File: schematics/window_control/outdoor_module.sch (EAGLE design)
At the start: 25 parts, among them J1 J_SMD, J10 USBASP_PIN, J2 J_SMD, J3 J_SMD, U5 BMP280 5V module, U6 LM317L, U7 LM358, U8 ATMEGA328P, U9 GY-SGP30

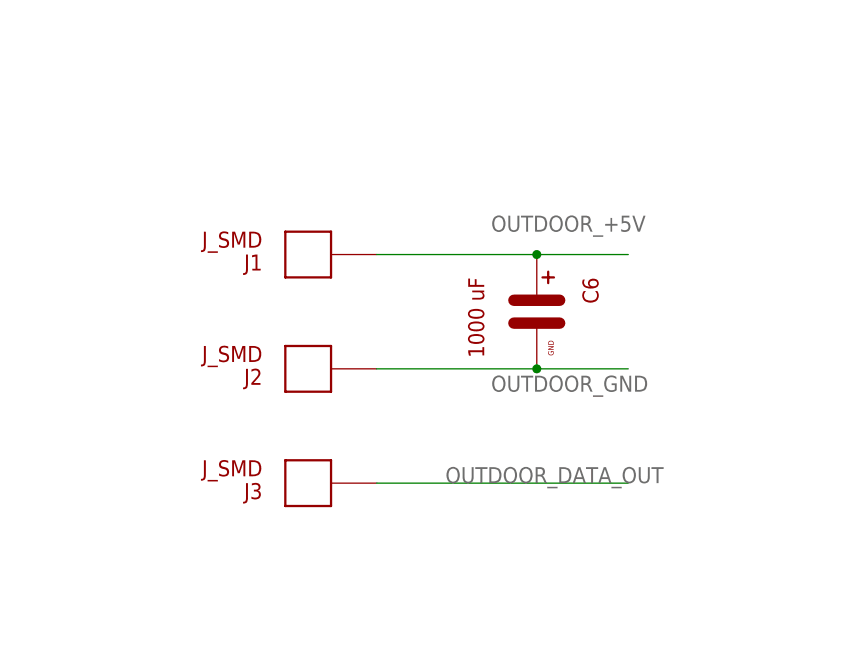
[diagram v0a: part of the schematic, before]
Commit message: Connectors changed
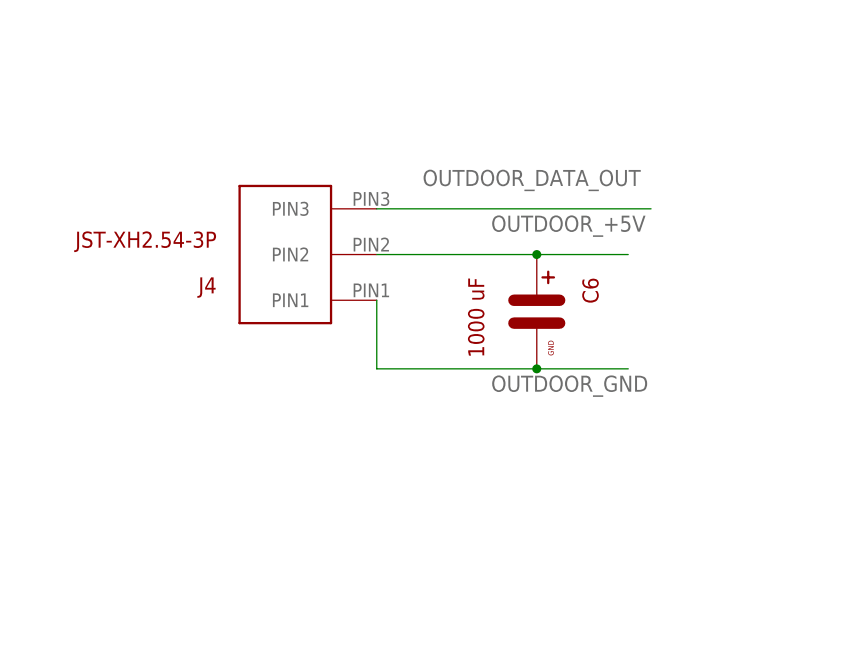
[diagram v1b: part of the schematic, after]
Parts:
- removed J1, J2, J3: J_SMD, my_devices:J_SMD
- added J4: JST-XH2.54-3P, my_devices:JST-XH254-3P
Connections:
- net OUTDOOR_+5V: now also J4.PIN2; no longer J1.PIN
- net OUTDOOR_DATA_OUT: now also J4.PIN3; no longer J3.PIN
- net OUTDOOR_GND: now also J4.PIN1; no longer J2.PIN
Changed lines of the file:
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@@
 <part name="C9" library="my_devices" deviceset="C-1" device="" value="0.1 uF"/>
 <part name="J10" library="my_devices" deviceset="USBASP_PIN" device=""/>
-<part name="J1" library="my_devices" deviceset="J_SMD" device=""/>
-<part name="J2" library="my_devices" deviceset="J_SMD" device=""/>
-<part name="J3" library="my_devices" deviceset="J_SMD" device=""/>
+<part name="J4" library="my_devices" deviceset="JST-XH254-3P" device="" value="JST-XH2.54-3P"/>
 </parts>
 <sheets>
@@
 <attribute name="VALUE" x="-103.505" y="208.915" size="0.8128" layer="94"/>
 </instance>
-<instance part="J1" gate="G$1" x="-297.18" y="264.16" smashed="yes" rot="R180" grouprefs="INPUT_CONNECTOR">
-<attribute name="NAME" x="-302.26" y="264.16" size="1.778" layer="94" rot="R180"/>
-<attribute name="VALUE" x="-302.26" y="266.7" size="1.778" layer="94" rot="R180"/>
-</instance>
-<instance part="J2" gate="G$1" x="-297.18" y="251.46" smashed="yes" rot="R180" grouprefs="INPUT_CONNECTOR">
-<attribute name="NAME" x="-302.26" y="251.46" size="1.778" layer="94" rot="R180"/>
-<attribute name="VALUE" x="-302.26" y="254" size="1.778" layer="94" rot="R180"/>
-</instance>
-<instance part="J3" gate="G$1" x="-297.18" y="238.76" smashed="yes" rot="R180" grouprefs="INPUT_CONNECTOR">
-<attribute name="NAME" x="-302.26" y="238.76" size="1.778" layer="94" rot="R180"/>
-<attribute name="VALUE" x="-302.26" y="241.3" size="1.778" layer="94" rot="R180"/>
+<instance part="J4" gate="G$1" x="-294.64" y="264.16" smashed="yes" rot="R180" grouprefs="INPUT_CONNECTOR">
+<attribute name="NAME" x="-307.34" y="261.62" size="1.778" layer="94" rot="R180"/>
+<attribute name="VALUE" x="-307.34" y="266.7" size="1.778" layer="94" rot="R180"/>
 </instance>
 </instances>
@@
 <junction x="-271.78" y="264.16" grouprefs="INPUT_CONNECTOR"/>
 <label x="-276.86" y="266.7" size="1.778" layer="95" grouprefs="INPUT_CONNECTOR"/>
-<pinref part="J1" gate="G$1" pin="PIN"/>
+<pinref part="J4" gate="G$1" pin="PIN2"/>
 </segment>
 <segment>
@@
 <junction x="-271.78" y="251.46" grouprefs="INPUT_CONNECTOR"/>
 <label x="-276.86" y="248.92" size="1.778" layer="95" grouprefs="INPUT_CONNECTOR"/>
-<pinref part="J2" gate="G$1" pin="PIN"/>
+<pinref part="J4" gate="G$1" pin="PIN1"/>
+<wire x1="-289.56" y1="259.08" x2="-289.56" y2="251.46" width="0.1524" layer="91" grouprefs="INPUT_CONNECTOR"/>
 </segment>
 <segment>
@@
 <net name="OUTDOOR_DATA_OUT" class="0">
 <segment>
-<wire x1="-289.56" y1="238.76" x2="-261.62" y2="238.76" width="0.1524" layer="91" grouprefs="INPUT_CONNECTOR"/>
-<label x="-281.94" y="238.76" size="1.778" layer="95" grouprefs="INPUT_CONNECTOR"/>
-<pinref part="J3" gate="G$1" pin="PIN"/>
-</segment>
-<segment>
+<wire x1="-289.56" y1="269.24" x2="-259.08" y2="269.24" width="0.1524" layer="91" grouprefs="INPUT_CONNECTOR"/>
+<label x="-284.48" y="271.78" size="1.778" layer="95" grouprefs="INPUT_CONNECTOR"/>
+<pinref part="J4" gate="G$1" pin="PIN3"/>
+</segment>
+<segment>

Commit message: Outdoor module board size reduced
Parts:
- U5: device my_devices:BME280 -> my_devices:BME280BME280-CONNECTOR-ONLY
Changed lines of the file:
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@@
 <grid distance="0.1" unitdist="inch" unit="inch" style="lines" multiple="1" display="no" altdistance="0.01" altunitdist="inch" altunit="inch"/>
 <layers>
-<layer number="1" name="Top" color="4" fill="1" visible="no" active="no"/>
-<layer number="2" name="Route2" color="1" fill="3" visible="no" active="no"/>
-<layer number="3" name="Route3" color="4" fill="3" visible="no" active="no"/>
-<layer number="4" name="Route4" color="1" fill="4" visible="no" active="no"/>
-<layer number="5" name="Route5" color="4" fill="4" visible="no" active="no"/>
-<layer number="6" name="Route6" color="1" fill="8" visible="no" active="no"/>
-<layer number="7" name="Route7" color="4" fill="8" visible="no" active="no"/>
-<layer number="8" name="Route8" color="1" fill="2" visible="no" active="no"/>
-<layer number="9" name="Route9" color="4" fill="2" visible="no" active="no"/>
-<layer number="10" name="Route10" color="1" fill="7" visible="no" active="no"/>
-<layer number="11" name="Route11" color="4" fill="7" visible="no" active="no"/>
-<layer number="12" name="Route12" color="1" fill="5" visible="no" active="no"/>
-<layer number="13" name="Route13" color="4" fill="5" visible="no" active="no"/>
-<layer number="14" name="Route14" color="1" fill="6" visible="no" active="no"/>
-<layer number="15" name="Route15" color="4" fill="6" visible="no" active="no"/>
-<layer number="16" name="Bottom" color="1" fill="1" visible="no" active="no"/>
-<layer number="17" name="Pads" color="2" fill="1" visible="no" active="no"/>
-<layer number="18" name="Vias" color="2" fill="1" visible="no" active="no"/>
-<layer number="19" name="Unrouted" color="6" fill="1" visible="no" active="no"/>
-<layer number="20" name="Dimension" color="24" fill="1" visible="no" active="no"/>
-<layer number="21" name="tPlace" color="7" fill="1" visible="no" active="no"/>
-<layer number="22" name="bPlace" color="7" fill="1" visible="no" active="no"/>
-<layer number="23" name="tOrigins" color="15" fill="1" visible="no" active="no"/>
-<layer number="24" name="bOrigins" color="15" fill="1" visible="no" active="no"/>
-<layer number="25" name="tNames" color="7" fill="1" visible="no" active="no"/>
-<layer number="26" name="bNames" color="7" fill="1" visible="no" active="no"/>
-<layer number="27" name="tValues" color="7" fill="1" visible="no" active="no"/>
-<layer number="28" name="bValues" color="7" fill="1" visible="no" active="no"/>
+<layer number="1" name="Top" color="4" fill="1" visible="yes" active="no"/>
+<layer number="2" name="Route2" color="16" fill="1" visible="yes" active="no"/>
+<layer number="3" name="Route3" color="17" fill="1" visible="yes" active="no"/>
+<layer number="4" name="Route4" color="18" fill="1" visible="yes" active="no"/>
+<layer number="5" name="Route5" color="19" fill="1" visible="yes" active="no"/>
+<layer number="6" name="Route6" color="25" fill="1" visible="yes" active="no"/>
+<layer number="7" name="Route7" color="26" fill="1" visible="yes" active="no"/>
+<layer number="8" name="Route8" color="27" fill="1" visible="yes" active="no"/>
+<layer number="9" name="Route9" color="28" fill="1" visible="yes" active="no"/>
+<layer number="10" name="Route10" color="29" fill="1" visible="yes" active="no"/>
+<layer number="11" name="Route11" color="30" fill="1" visible="yes" active="no"/>
+<layer number="12" name="Route12" color="20" fill="1" visible="yes" active="no"/>
+<layer number="13" name="Route13" color="21" fill="1" visible="yes" active="no"/>
+<layer number="14" name="Route14" color="22" fill="1" visible="yes" active="no"/>
+<layer number="15" name="Route15" color="23" fill="1" visible="yes" active="no"/>
+<layer number="16" name="Bottom" color="1" fill="1" visible="yes" active="no"/>
+<layer number="17" name="Pads" color="2" fill="1" visible="yes" active="no"/>
+<layer number="18" name="Vias" color="2" fill="1" visible="yes" active="no"/>
+<layer number="19" name="Unrouted" color="6" fill="1" visible="yes" active="no"/>
+<layer number="20" name="Dimension" color="24" fill="1" visible="yes" active="no"/>
+<layer number="21" name="tPlace" color="7" fill="1" visible="yes" active="no"/>
+<layer number="22" name="bPlace" color="7" fill="1" visible="yes" active="no"/>
+<layer number="23" name="tOrigins" color="15" fill="1" visible="yes" active="no"/>
+<layer number="24" name="bOrigins" color="15" fill="1" visible="yes" active="no"/>
+<layer number="25" name="tNames" color="7" fill="1" visible="yes" active="no"/>
+<layer number="26" name="bNames" color="7" fill="1" visible="yes" active="no"/>
+<layer number="27" name="tValues" color="7" fill="1" visible="yes" active="no"/>
+<layer number="28" name="bValues" color="7" fill="1" visible="yes" active="no"/>
 <layer number="29" name="tStop" color="7" fill="3" visible="no" active="no"/>
 <layer number="30" name="bStop" color="7" fill="6" visible="no" active="no"/>
@@
 <layer number="35" name="tGlue" color="7" fill="4" visible="no" active="no"/>
 <layer number="36" name="bGlue" color="7" fill="5" visible="no" active="no"/>
-<layer number="37" name="tTest" color="7" fill="1" visible="no" active="no"/>
-<layer number="38" name="bTest" color="7" fill="1" visible="no" active="no"/>
+<layer number="37" name="tTest" color="7" fill="1" visible="yes" active="no"/>
+<layer number="38" name="bTest" color="7" fill="1" visible="yes" active="no"/>
 <layer number="39" name="tKeepout" color="4" fill="11" visible="no" active="no"/>
 <layer number="40" name="bKeepout" color="1" fill="11" visible="no" active="no"/>
@@
 <layer number="44" name="Drills" color="7" fill="1" visible="no" active="no"/>
 <layer number="45" name="Holes" color="7" fill="1" visible="no" active="no"/>
-<layer number="46" name="Milling" color="3" fill="1" visible="no" active="no"/>
-<layer number="47" name="Measures" color="7" fill="1" visible="no" active="no"/>
-<layer number="48" name="Document" color="7" fill="1" visible="no" active="no"/>
-<layer number="49" name="Reference" color="7" fill="1" visible="no" active="no"/>
-<layer number="51" name="tDocu" color="7" fill="1" visible="no" active="no"/>
-<layer number="52" name="bDocu" color="7" fill="1" visible="no" active="no"/>
+<layer number="46" name="Milling" color="3" fill="1" visible="yes" active="no"/>
+<layer number="47" name="Measures" color="7" fill="1" visible="yes" active="no"/>
+<layer number="48" name="Document" color="7" fill="1" visible="yes" active="no"/>
+<layer number="49" name="Reference" color="7" fill="1" visible="yes" active="no"/>
+<layer number="51" name="tDocu" color="7" fill="1" visible="yes" active="no"/>
+<layer number="52" name="bDocu" color="7" fill="1" visible="yes" active="no"/>
 <layer number="88" name="SimResults" color="9" fill="1" visible="yes" active="yes"/>
 <layer number="89" name="SimProbes" color="9" fill="1" visible="yes" active="yes"/>
@@
 <parts>
 <part name="R21" library="my_devices" deviceset="R" device="" value="10K"/>
-<part name="U5" library="my_devices" deviceset="BME280" device="" value="BMP280 5V module"/>
+<part name="U5" library="my_devices" deviceset="BME280" device="BME280-CONNECTOR-ONLY" value="BMP280 5V module"/>
 <part name="U9" library="my_devices" deviceset="GY-SGP30" device=""/>
 <part name="C6" library="my_devices" deviceset="C" device="" value="1000 uF"/>

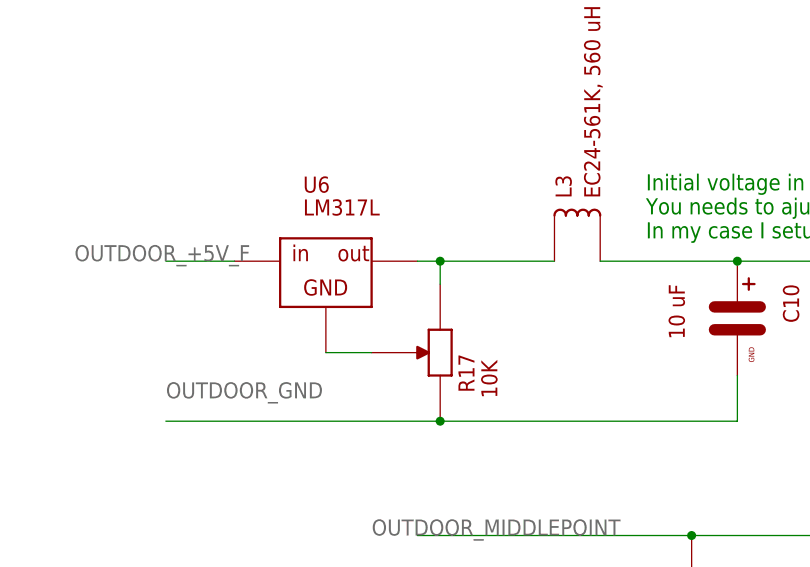
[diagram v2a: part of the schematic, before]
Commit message: fixed error in outdoor board and schema
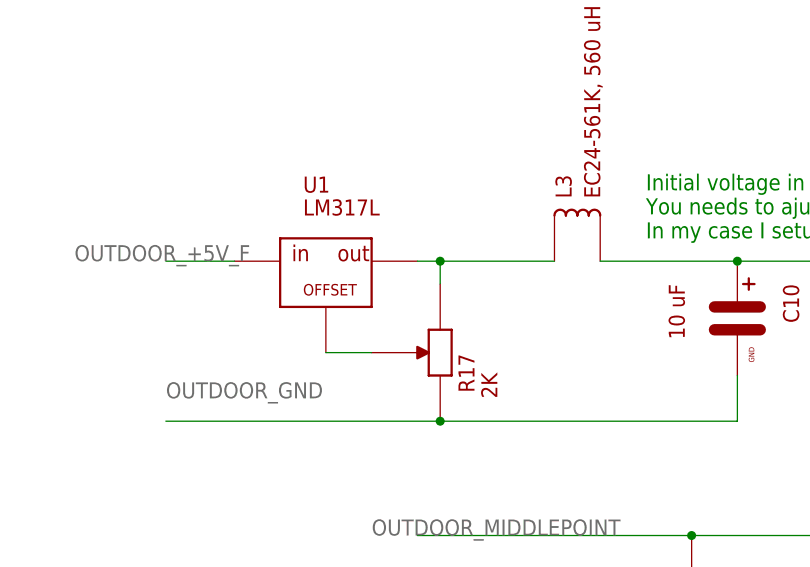
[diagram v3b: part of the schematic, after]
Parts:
- removed U6: LM317L, my_devices:VOLTAGE_REGULATOR
- added U1: LM317L, my_devices:LM317L
- R17: value 10K -> 2K
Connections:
- net N$17: now also U1.GND; no longer U6.GND
- net OUT: now also U1.OUT; no longer U6.OUT
- net OUTDOOR_+5V_F: now also U1.IN; no longer U6.IN

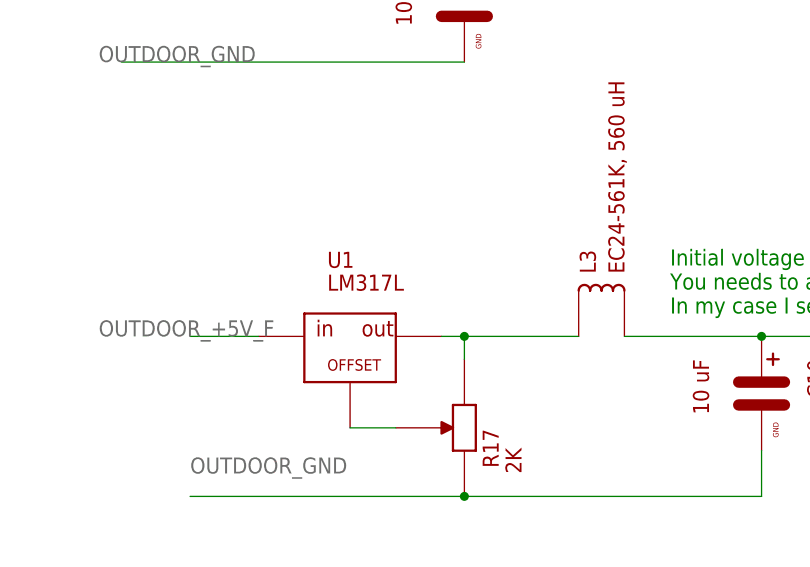
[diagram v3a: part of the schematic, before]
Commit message: actualized voltage regulator nominal
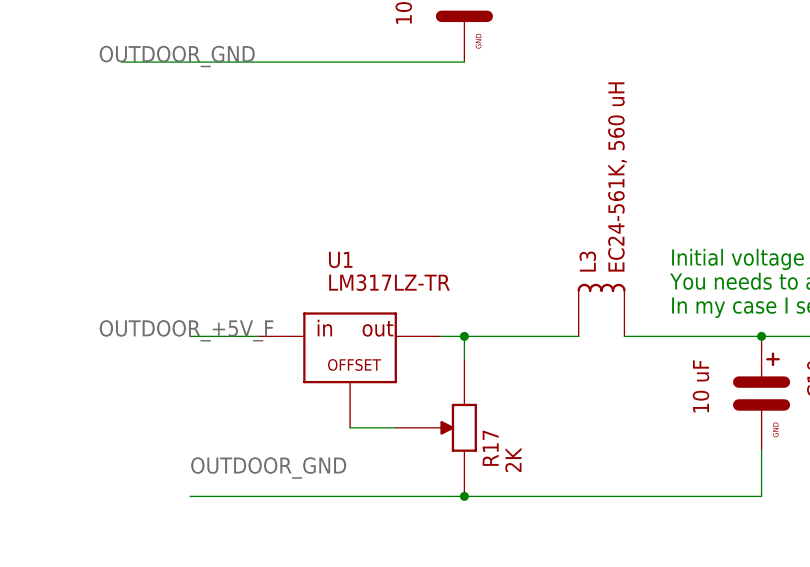
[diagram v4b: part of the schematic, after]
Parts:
- U1: value LM317L -> LM317LZ-TR
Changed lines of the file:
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@@
 <part name="J10" library="my_devices" deviceset="USBASP_PIN" device=""/>
 <part name="J4" library="my_devices" deviceset="JST-XH254-3P" device="" value="JST-XH2.54-3P"/>
-<part name="U1" library="my_devices" deviceset="LM317L" device=""/>
+<part name="U1" library="my_devices" deviceset="LM317L" device="" value="LM317LZ-TR"/>
 </parts>
 <sheets>
